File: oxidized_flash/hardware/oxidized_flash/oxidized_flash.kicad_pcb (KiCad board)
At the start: 2 copper layers, 61 x 21.6 mm, 37 parts, among them J1 USB_A, J2 Conn_ARM_JTAG_SWD_10, U1 LM1117-3.3, U2 ATSAMD51G18A-MU, U3 IS21ES

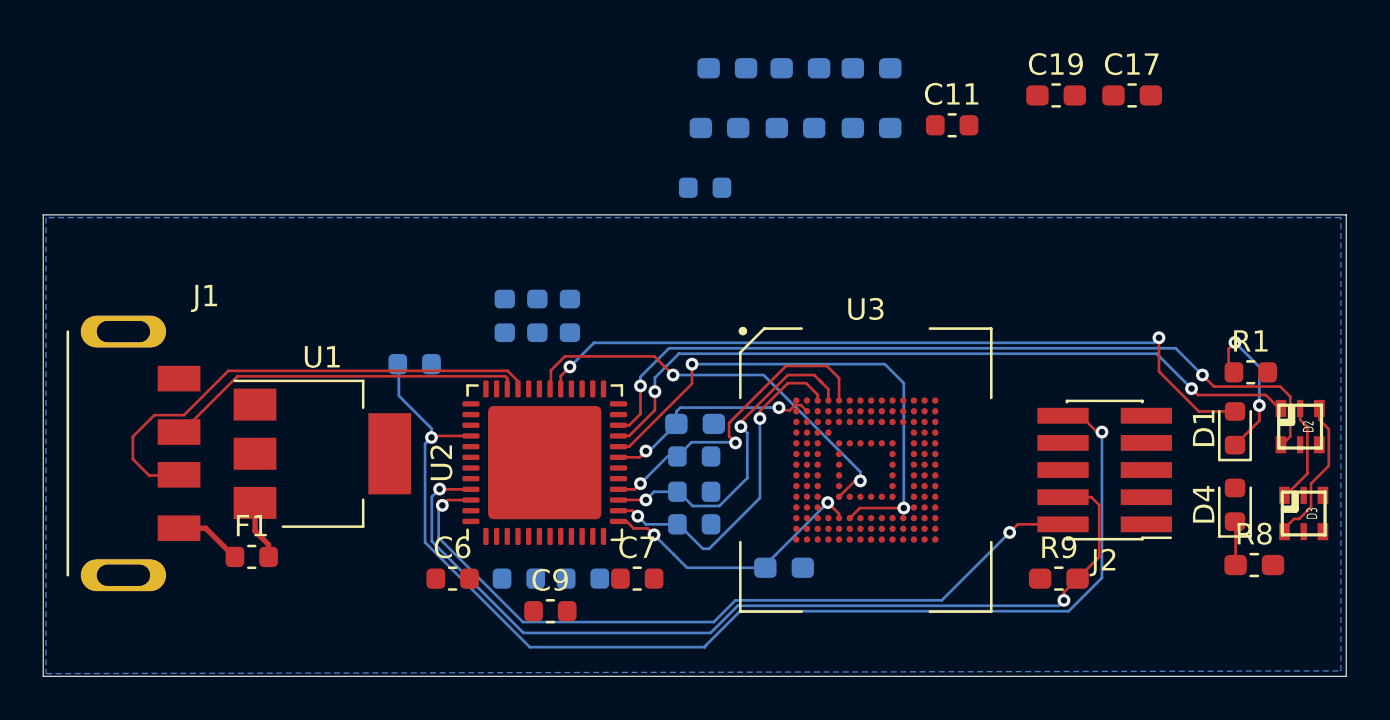
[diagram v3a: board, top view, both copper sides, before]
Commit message: Rip out all the emmc stuff, just a samd with lights
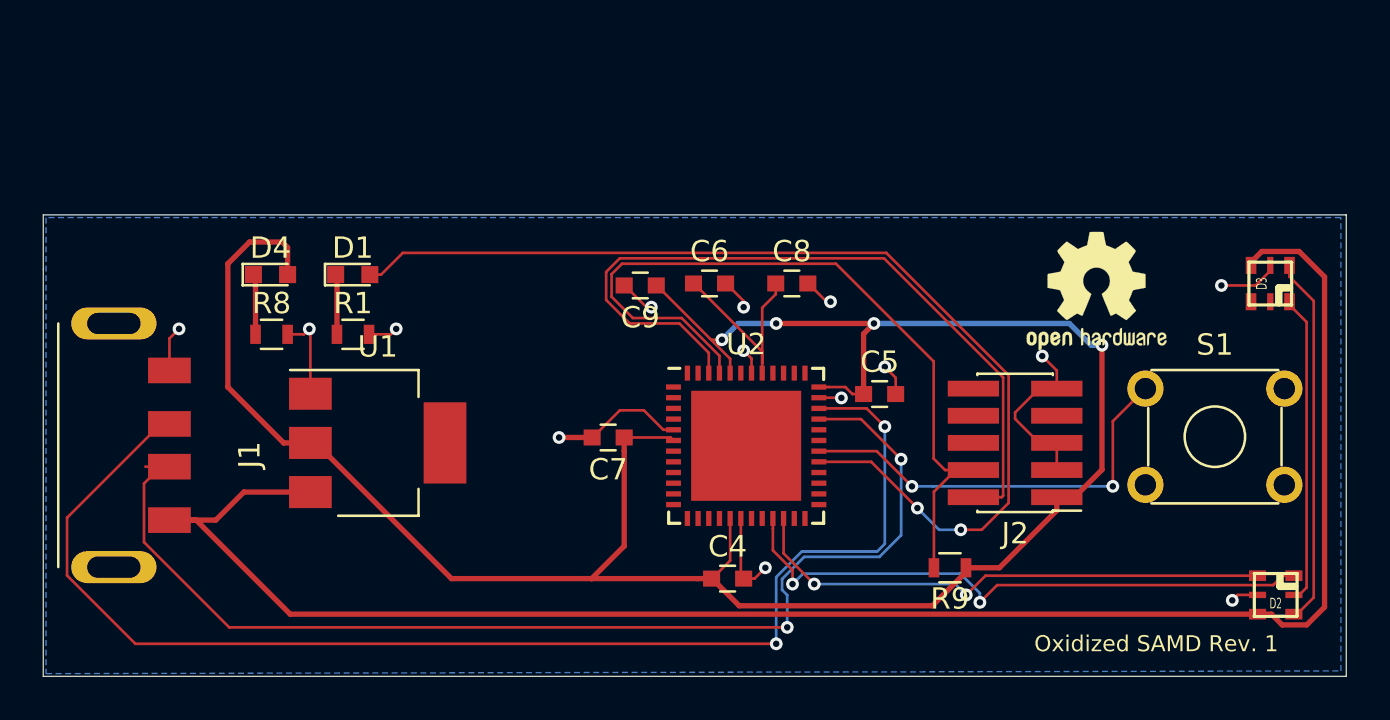
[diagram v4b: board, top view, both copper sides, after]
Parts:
- removed C10, C11: 3u, Capacitor_SMD:C_0603_1608Metric
- removed C12, C13, C14, C15, C16, C17, C18, C19: 3u, Capacitor_SMD:C_0603_1608Metric_Pad1.05x0.95mm_HandSolder
- removed C3: 0.1u, Capacitor_SMD:C_0603_1608Metric
- removed F1: 500mA, Fuse:Fuse_0603_1608Metric
- removed L1: 10uH, Inductor_SMD:L_0603_1608Metric
- removed R2: 1k, Resistor_SMD:R_0603_1608Metric
- removed R3, R4, R5: 10K, Resistor_SMD:R_0603_1608Metric
- removed R6, R7: 10K, Resistor_SMD:R_0603_1608Metric_Pad1.05x0.95mm_HandSolder
- removed U3: IS21ES, Custom_BGA:FBGA-153_14x14_11.5x13.0mm
- added REF***: OSHW-Logo2_7.3x6mm_SilkScreen, Symbols:OSHW-Logo2_7.3x6mm_SilkScreen, F.Cu at (73.4, 23.9)
- added S1: B3F-1000, Buttons_Switches_THT:SW_TH_Tactile_Omron_B3F-10xx, F.Cu at (75.7, 28.4)
- C4, C5, C8: footprint Capacitor_SMD:C_0603_1608Metric -> Capacitors_SMD:C_0603; moved to F.Cu
- C6, C7, C9: footprint Capacitor_SMD:C_0603_1608Metric -> Capacitors_SMD:C_0603
- D1, D4: footprint LED_SMD:LED_0603_1608Metric -> LEDs:LED_0603
- J2: footprint Connector_PinHeader_1.27mm:PinHeader_2x05_P1.27mm_Vertical_SMD -> Pin_Headers:Pin_Header_Straight_2x05_Pitch1.27mm_SMD
- R1: footprint Resistor_SMD:R_0603_1608Metric -> Resistors_SMD:R_0603
- R8, R9: footprint Resistor_SMD:R_0603_1608Metric_Pad1.05x0.95mm_HandSolder -> Resistors_SMD:R_0603
- U1: footprint Package_TO_SOT_SMD:SOT-223 -> TO_SOT_Packages_SMD:SOT-223
- U2: footprint Package_DFN_QFN:QFN-48-1EP_7x7mm_P0.5mm_EP5.3x5.3mm -> Housings_DFN_QFN:QFN-48-1EP_7x7mm_Pitch0.5mm
- moved R8 47.2 mm to (34.8, 25.9)
- moved D4 46.4 mm to (34.8, 23.1), turned to 0 degrees
- moved R1 42.0 mm to (38.6, 25.9)
- moved D1 41.9 mm to (38.6, 23.1), turned to 0 degrees
- moved C5 19.0 mm to (63.3, 28.7), turned to 0 degrees
- moved C6 18.3 mm to (55.3, 23.5)
- moved C9 15.8 mm to (52.1, 23.6), turned to 180 degrees
- moved D3 10.9 mm to (81.5, 23.5), turned to 270 degrees
- moved C8 10.5 mm to (59.1, 23.5), turned to 0 degrees
- moved U2 9.46 mm to (57.0, 31.1), turned to 0 degrees
- moved D2 7.96 mm to (81.8, 38.1), turned to 0 degrees
- moved C4 6.77 mm to (56.1, 37.3)
- moved C7 6.74 mm to (50.6, 30.7), turned to 180 degrees
- moved R9 5.12 mm to (66.5, 36.8), turned to 180 degrees
- moved J2 4.38 mm to (69.6, 31.0)
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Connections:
- U1 pad 3: Net-(F1-Pad2) -> +5V
- U2 pad 30: /MC_RST -> /PA21
- U2 pad 40: /SWD_RST -> Net-(U2-Pad40)
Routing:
- net +3V3: track 0.00 -> 107.5 mm, vias 0 -> 4
- net +5V: track 3.22 -> 83.3 mm
- net /SWD_RST: track 55.0 -> 0.00 mm, vias 2 -> 0
- net Net-(J1-Pad3): track 17.0 -> 61.6 mm, vias 0 -> 2
- net GND: track 0.22 -> 38.7 mm, vias 0 -> 14
- net Net-(J1-Pad2): track 23.9 -> 54.1 mm, vias 0 -> 2
- net Net-(U2-Pad20): track 24.4 -> 0.00 mm, vias 2 -> 0
- net /MC_RST: track 19.7 -> 0.00 mm, vias 2 -> 0
- net /PA21: track 0.00 -> 19.6 mm, vias 0 -> 2
- net Net-(U2-Pad14): track 16.1 -> 0.00 mm, vias 2 -> 0
- net Net-(U2-Pad15): track 15.8 -> 0.00 mm, vias 2 -> 0
- net Net-(U2-Pad16): track 14.9 -> 0.00 mm, vias 2 -> 0
- net /PA20: track 35.2 -> 49.4 mm
- net Net-(U2-Pad13): track 13.3 -> 0.00 mm, vias 2 -> 0
- net /SCK: track 37.3 -> 25.0 mm
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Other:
- board text added: "Oxidized SAMD Rev. 1"

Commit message: Add 512M SPI flash
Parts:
- added C1: 0.1u, Capacitors_SMD:C_0603, F.Cu at (44.5, 24.1)
- added U3: MT25QL, Housings_SSOP:SOP-16_4.4x10.4mm_Pitch1.27mm, F.Cu at (47.2, 31.2)
- U2: value ATSAMD51G18A-MU -> ATSAMD51G19A-MU
- moved C7 7.08 mm to (48.0, 24.1)
- moved U1 2.45 mm to (37.3, 31.2)
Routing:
- net Net-(U2-Pad19): track 0.00 -> 22.5 mm, vias 0 -> 4
- net Net-(U2-Pad20): track 0.00 -> 21.4 mm, vias 0 -> 2
- net Net-(U2-Pad16): track 0.00 -> 21.3 mm, vias 0 -> 2
- net +3V3: track 107.5 -> 124.4 mm
- net GND: track 38.7 -> 51.4 mm, vias 14 -> 15
- net Net-(U2-Pad14): track 0.00 -> 12.0 mm
- net Net-(U2-Pad13): track 0.00 -> 10.5 mm
- net Net-(U2-Pad15): track 0.00 -> 5.95 mm
- net +5V: track 83.3 -> 79.6 mm
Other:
- board text added: "Oxidized Flash Rev. 1"
- board text removed: "Oxidized SAMD Rev. 1"

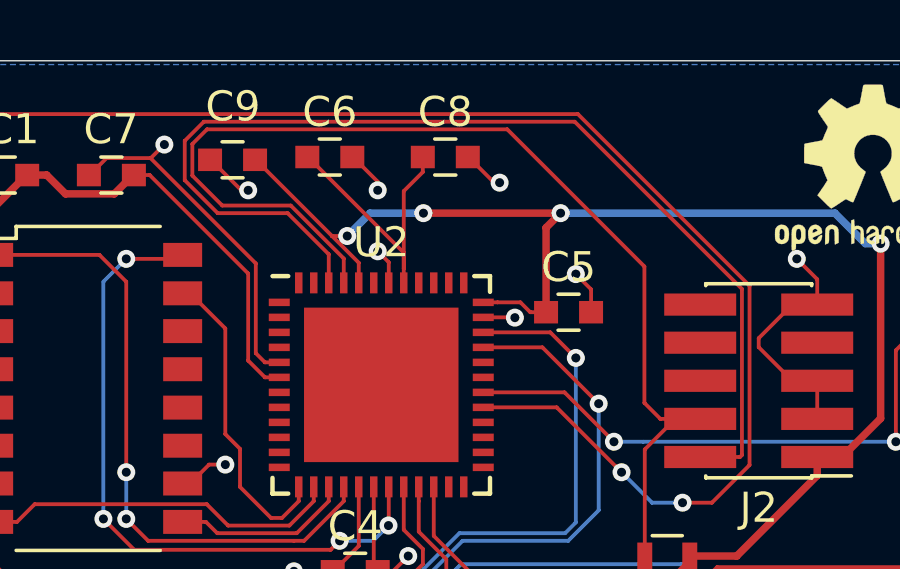
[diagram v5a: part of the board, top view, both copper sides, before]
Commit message: Fixup decoupling capacitors on the SAMD
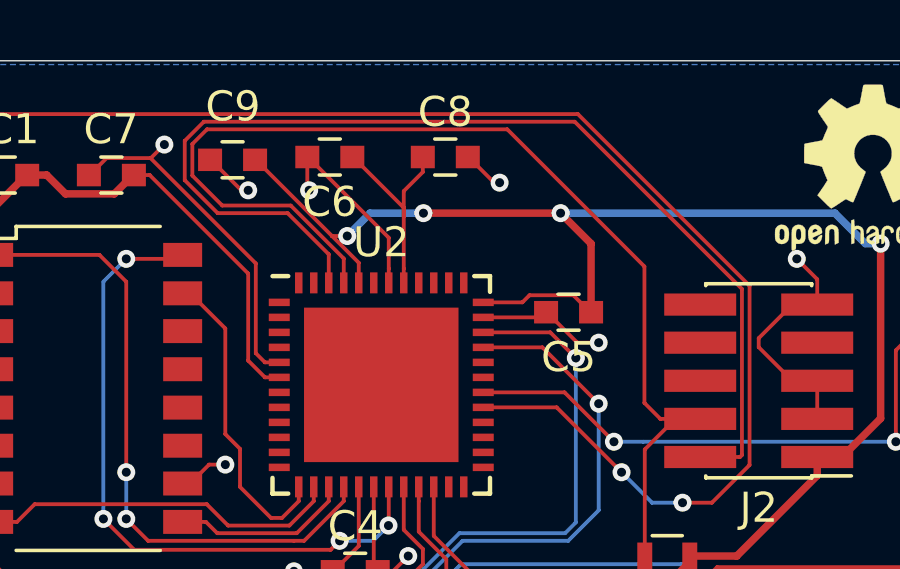
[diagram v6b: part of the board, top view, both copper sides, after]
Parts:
- turned C5 to 180 degrees
- turned C6 to 180 degrees
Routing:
- net GND: track 51.4 -> 57.0 mm, vias 15 -> 13
- net Net-(C6-Pad1): track 9.52 -> 7.16 mm
- net +3V3: track 124.4 -> 126.3 mm
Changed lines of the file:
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@@
     (thickness 1.6)
     (drawings 6)
-    (tracks 332)
+    (tracks 334)
     (zones 0)
     (modules 21)
@@
   )
   (setup
-    (last_trace_width 0.25)
+    (last_trace_width 0.127)
     (user_trace_width 0.127)
     (trace_clearance 0.127)
@@
   )
   (module Capacitors_SMD:C_0603 (layer F.Cu)
-    (at 63.258 28.702)
+    (at 63.258 28.702 180)
     (descr "Capacitor SMD 0603, reflow soldering, AVX (see smccp.pdf)")
     (tags "capacitor 0603")
@@
     (fp_line (start 1.4 0.65) (end 1.4 -0.65) (layer F.CrtYd) (width 0.05))
     (fp_line (start 1.4 0.65) (end -1.4 0.65) (layer F.CrtYd) (width 0.05))
-    (pad 1 smd rect (at -0.75 0) (size 0.8 0.75) (layers F.Cu F.Paste F.Mask)
+    (pad 1 smd rect (at -0.75 0 180) (size 0.8 0.75) (layers F.Cu F.Paste F.Mask)
       (net 3 +3V3))
-    (pad 2 smd rect (at 0.75 0) (size 0.8 0.75) (layers F.Cu F.Paste F.Mask)
+    (pad 2 smd rect (at 0.75 0 180) (size 0.8 0.75) (layers F.Cu F.Paste F.Mask)
       (net 1 GND))
     (model Capacitors_SMD.3dshapes/C_0603.wrl
@@
   )
   (module Capacitors_SMD:C_0603 (layer F.Cu)
-    (at 55.299001 23.529001)
+    (at 55.299001 23.529001 180)
     (descr "Capacitor SMD 0603, reflow soldering, AVX (see smccp.pdf)")
     (tags "capacitor 0603")
@@
     (fp_line (start 1.4 0.65) (end 1.4 -0.65) (layer F.CrtYd) (width 0.05))
     (fp_line (start 1.4 0.65) (end -1.4 0.65) (layer F.CrtYd) (width 0.05))
-    (pad 1 smd rect (at -0.75 0) (size 0.8 0.75) (layers F.Cu F.Paste F.Mask)
+    (pad 1 smd rect (at -0.75 0 180) (size 0.8 0.75) (layers F.Cu F.Paste F.Mask)
       (net 4 "Net-(C6-Pad1)"))
-    (pad 2 smd rect (at 0.75 0) (size 0.8 0.75) (layers F.Cu F.Paste F.Mask)
+    (pad 2 smd rect (at 0.75 0 180) (size 0.8 0.75) (layers F.Cu F.Paste F.Mask)
       (net 1 GND))
     (model Capacitors_SMD.3dshapes/C_0603.wrl
@@
   (segment (start 69.596 29.568) (end 70.716 28.448) (width 0.127) (layer F.Cu) (net 1))
   (segment (start 69.596 29.868) (end 69.596 29.568) (width 0.127) (layer F.Cu) (net 1))
-  (via (at 56.896 24.638) (size 0.6) (drill 0.3) (layers F.Cu B.Cu) (net 1))
-  (segment (start 56.896 24.351) (end 56.896 24.638) (width 0.127) (layer F.Cu) (net 1))
-  (segment (start 56.049001 23.529001) (end 56.074001 23.529001) (width 0.127) (layer F.Cu) (net 1))
-  (segment (start 56.074001 23.529001) (end 56.896 24.351) (width 0.127) (layer F.Cu) (net 1))
   (via (at 60.96 24.384) (size 0.6) (drill 0.3) (layers F.Cu B.Cu) (net 1))
   (segment (start 60.779 24.384) (end 60.96 24.384) (width 0.127) (layer F.Cu) (net 1))
   (segment (start 59.899001 23.529001) (end 59.924001 23.529001) (width 0.127) (layer F.Cu) (net 1))
   (segment (start 59.924001 23.529001) (end 60.779 24.384) (width 0.127) (layer F.Cu) (net 1))
-  (via (at 56.896 26.67) (size 0.6) (drill 0.3) (layers F.Cu B.Cu) (net 1))
-  (segment (start 57.26425 27.72375) (end 57.26425 27.03825) (width 0.127) (layer F.Cu) (net 1))
-  (segment (start 57.26425 27.03825) (end 56.896 26.67) (width 0.127) (layer F.Cu) (net 1))
-  (via (at 61.468 28.88325) (size 0.6) (drill 0.3) (layers F.Cu B.Cu) (net 1))
-  (segment (start 60.41425 28.87375) (end 61.4585 28.87375) (width 0.127) (layer F.Cu) (net 1))
-  (segment (start 61.4585 28.87375) (end 61.468 28.88325) (width 0.127) (layer F.Cu) (net 1))
-  (via (at 63.5 27.432) (size 0.6) (drill 0.3) (layers F.Cu B.Cu) (net 1))
-  (segment (start 64.008 28.702) (end 64.008 27.94) (width 0.127) (layer F.Cu) (net 1))
-  (segment (start 64.008 27.94) (end 63.5 27.432) (width 0.127) (layer F.Cu) (net 1))
   (via (at 79.756 38.354) (size 0.6) (drill 0.3) (layers F.Cu B.Cu) (net 1))
   (segment (start 80.938 38.1) (end 80.01 38.1) (width 0.127) (layer F.Cu) (net 1))
@@
   (segment (start 30.032 27.6) (end 30.032 26.864) (width 0.25) (layer F.Cu) (net 1))
   (segment (start 30.032 26.864) (end 30.734 26.162) (width 0.25) (layer F.Cu) (net 1))
+  (segment (start 62.33625 28.87375) (end 62.508 28.702) (width 0.127) (layer F.Cu) (net 1))
+  (segment (start 60.41425 28.87375) (end 62.33625 28.87375) (width 0.127) (layer F.Cu) (net 1))
+  (segment (start 57.26425 27.24675) (end 57.26425 27.72375) (width 0.127) (layer F.Cu) (net 1))
+  (segment (start 57.26425 26.21925) (end 57.26425 27.24675) (width 0.127) (layer F.Cu) (net 1))
+  (segment (start 54.574001 23.529001) (end 57.26425 26.21925) (width 0.127) (layer F.Cu) (net 1))
+  (segment (start 54.549001 23.529001) (end 54.574001 23.529001) (width 0.127) (layer F.Cu) (net 1))
+  (via (at 54.61 24.638) (size 0.6) (drill 0.3) (layers F.Cu B.Cu) (net 1))
+  (segment (start 54.549001 23.529001) (end 54.549001 24.577001) (width 0.127) (layer F.Cu) (net 1))
+  (segment (start 54.549001 24.577001) (end 54.61 24.638) (width 0.127) (layer F.Cu) (net 1))
+  (via (at 64.262 29.718) (size 0.6) (drill 0.3) (layers F.Cu B.Cu) (net 1))
+  (segment (start 63.549 29.718) (end 64.262 29.718) (width 0.127) (layer F.Cu) (net 1))
+  (segment (start 62.508 28.702) (end 62.533 28.702) (width 0.127) (layer F.Cu) (net 1))
+  (segment (start 62.533 28.702) (end 63.549 29.718) (width 0.127) (layer F.Cu) (net 1))
   (segment (start 55.421 37.338) (end 55.396 37.338) (width 0.127) (layer F.Cu) (net 3))
   (segment (start 56.26425 36.49475) (end 55.421 37.338) (width 0.127) (layer F.Cu) (net 3))
@@
   (segment (start 52.833 23.622) (end 52.808 23.622) (width 0.127) (layer F.Cu) (net 3))
   (segment (start 56.26425 27.72375) (end 56.26425 27.05325) (width 0.127) (layer F.Cu) (net 3))
-  (segment (start 60.89125 28.37375) (end 60.41425 28.37375) (width 0.127) (layer F.Cu) (net 3))
-  (segment (start 61.65275 28.37375) (end 60.89125 28.37375) (width 0.127) (layer F.Cu) (net 3))
-  (segment (start 61.981 28.702) (end 61.65275 28.37375) (width 0.127) (layer F.Cu) (net 3))
-  (segment (start 62.508 28.702) (end 61.981 28.702) (width 0.127) (layer F.Cu) (net 3))
   (segment (start 55.421 37.338) (end 56.691 38.608) (width 0.25) (layer F.Cu) (net 3))
   (segment (start 65.72 38.608) (end 67.298 37.03) (width 0.25) (layer F.Cu) (net 3))
@@
   (segment (start 73.152 26.416) (end 72.136 25.4) (width 0.25) (layer B.Cu) (net 3))
   (segment (start 72.136 25.4) (end 62.992 25.4) (width 0.25) (layer B.Cu) (net 3))
-  (segment (start 62.508 25.884) (end 62.508 28.702) (width 0.25) (layer F.Cu) (net 3))
-  (segment (start 62.992 25.4) (end 62.508 25.884) (width 0.25) (layer F.Cu) (net 3))
   (via (at 58.42 25.4) (size 0.6) (drill 0.3) (layers F.Cu B.Cu) (net 3))
   (segment (start 62.992 25.4) (end 58.42 25.4) (width 0.25) (layer F.Cu) (net 3))
@@
   (segment (start 41.161001 37.965001) (end 54.743999 37.965001) (width 0.25) (layer F.Cu) (net 3))
   (segment (start 34.438 31.242) (end 41.161001 37.965001) (width 0.25) (layer F.Cu) (net 3))
-  (segment (start 57.76425 24.665752) (end 57.76425 27.24675) (width 0.127) (layer F.Cu) (net 4))
+  (segment (start 63.417499 28.136499) (end 63.983 28.702) (width 0.127) (layer F.Cu) (net 3))
+  (segment (start 61.955599 28.136499) (end 63.417499 28.136499) (width 0.127) (layer F.Cu) (net 3))
+  (segment (start 61.718348 28.37375) (end 61.955599 28.136499) (width 0.127) (layer F.Cu) (net 3))
+  (segment (start 60.41425 28.37375) (end 61.718348 28.37375) (width 0.127) (layer F.Cu) (net 3))
+  (segment (start 63.983 28.702) (end 64.008 28.702) (width 0.127) (layer F.Cu) (net 3))
+  (segment (start 64.008 26.416) (end 62.992 25.4) (width 0.25) (layer F.Cu) (net 3))
+  (segment (start 64.008 28.702) (end 64.008 26.416) (width 0.25) (layer F.Cu) (net 3))
   (segment (start 58.399001 24.031001) (end 57.76425 24.665752) (width 0.127) (layer F.Cu) (net 4))
   (segment (start 58.399001 23.529001) (end 58.399001 24.031001) (width 0.127) (layer F.Cu) (net 4))
   (segment (start 57.76425 27.24675) (end 57.76425 27.72375) (width 0.127) (layer F.Cu) (net 4))
-  (segment (start 57.76425 26.71925) (end 57.76425 27.24675) (width 0.127) (layer F.Cu) (net 4))
-  (segment (start 54.574001 23.529001) (end 57.76425 26.71925) (width 0.127) (layer F.Cu) (net 4))
-  (segment (start 54.549001 23.529001) (end 54.574001 23.529001) (width 0.127) (layer F.Cu) (net 4))
+  (segment (start 57.76425 25.21925) (end 57.76425 25.50625) (width 0.127) (layer F.Cu) (net 4))
+  (segment (start 56.074001 23.529001) (end 57.76425 25.21925) (width 0.127) (layer F.Cu) (net 4))
+  (segment (start 56.049001 23.529001) (end 56.074001 23.529001) (width 0.127) (layer F.Cu) (net 4))
+  (segment (start 57.76425 24.665752) (end 57.76425 25.50625) (width 0.127) (layer F.Cu) (net 4))
+  (segment (start 57.76425 25.50625) (end 57.76425 27.24675) (width 0.127) (layer F.Cu) (net 4))
   (via (at 67.056 35.052) (size 0.6) (drill 0.3) (layers F.Cu B.Cu) (net 5))
   (segment (start 68.034902 35.052) (end 67.056 35.052) (width 0.127) (layer F.Cu) (net 5))
